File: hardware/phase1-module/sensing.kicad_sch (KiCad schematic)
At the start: 0 parts

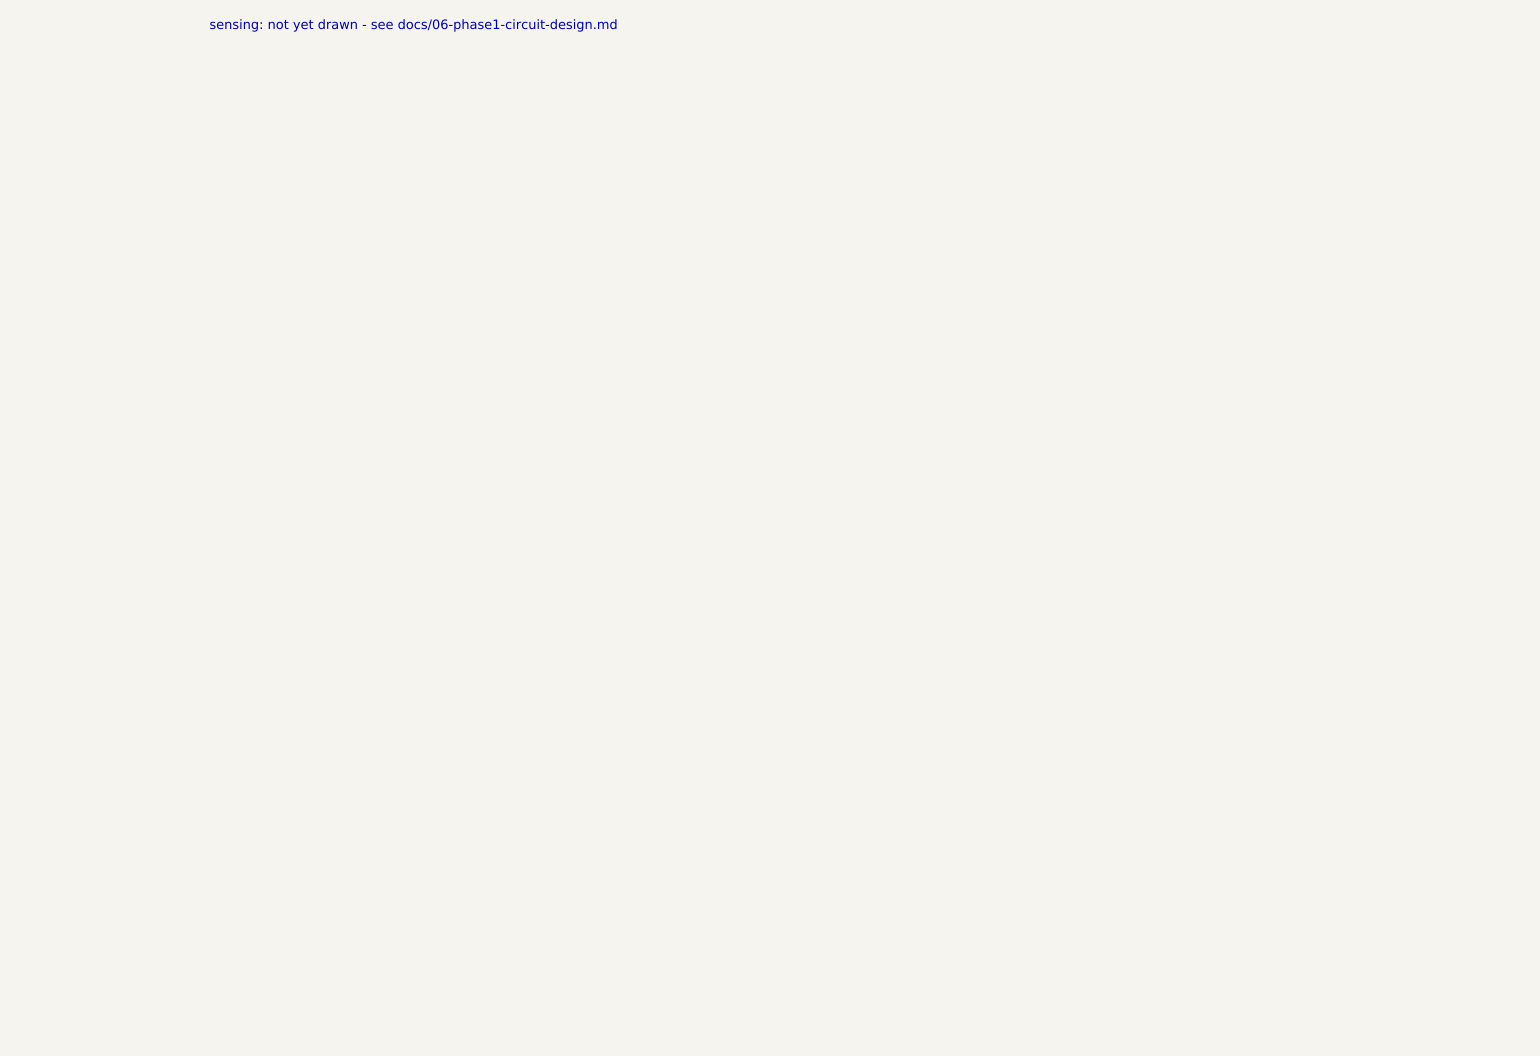
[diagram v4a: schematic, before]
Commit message: Complete Phase-1 schematic: all six remaining sheets, netlist-verified
- power-stage: LM5145 @350kHz (RT 28.7K per ds eq.3), RDS(on) valley
  ILIM 365R->SW, UVLO divider, EN kill chain (NOT(HW_EN) OR PS_OFF via
  Q5/Q6 + diode-OR), Type-III comp starting values, SYNCIN as DEM/FPWM
- sensing: 2m shunt, INA240A3 -> CC loop, INA228 telemetry, /8 divider,
  NT1 single AGND-PGND tie
- disconnect: back-to-back FETs + LTC7004, INP = OUT_REQ AND NOT(kill)
  AND NOT(OVP); TLV7011 + Q9 trips at 22.25V
- aux-rails: LMR36015 (5.016V) -> NCP1117 3V3
- mcu-can: STM32G431CBT6 fully pinned; I2C moved to I2C2/PA8-PA9 (PB8
  is the BOOT0 strap - pullup there would boot the ROM loader), BOOT0
  strapped low, OUT_REQ on PB14 (PB4 NJTRST reset pull-up), 8MHz
  crystal for CAN, TCAN1042 (VCC 5V, VIO 3V3)
- io: fused input + SMBJ33A TVS, output, backplane header, fan switch
  (1N4148W flyback orientation corrected: pin 1 = cathode)
- checker: duplicate-ref detection + global/local split-net detection;
  caught duplicate C62 and the LMR36015 FB-pin placement collision

Co-Authored-By: Claude Fable 5 <noreply@anthropic.com>
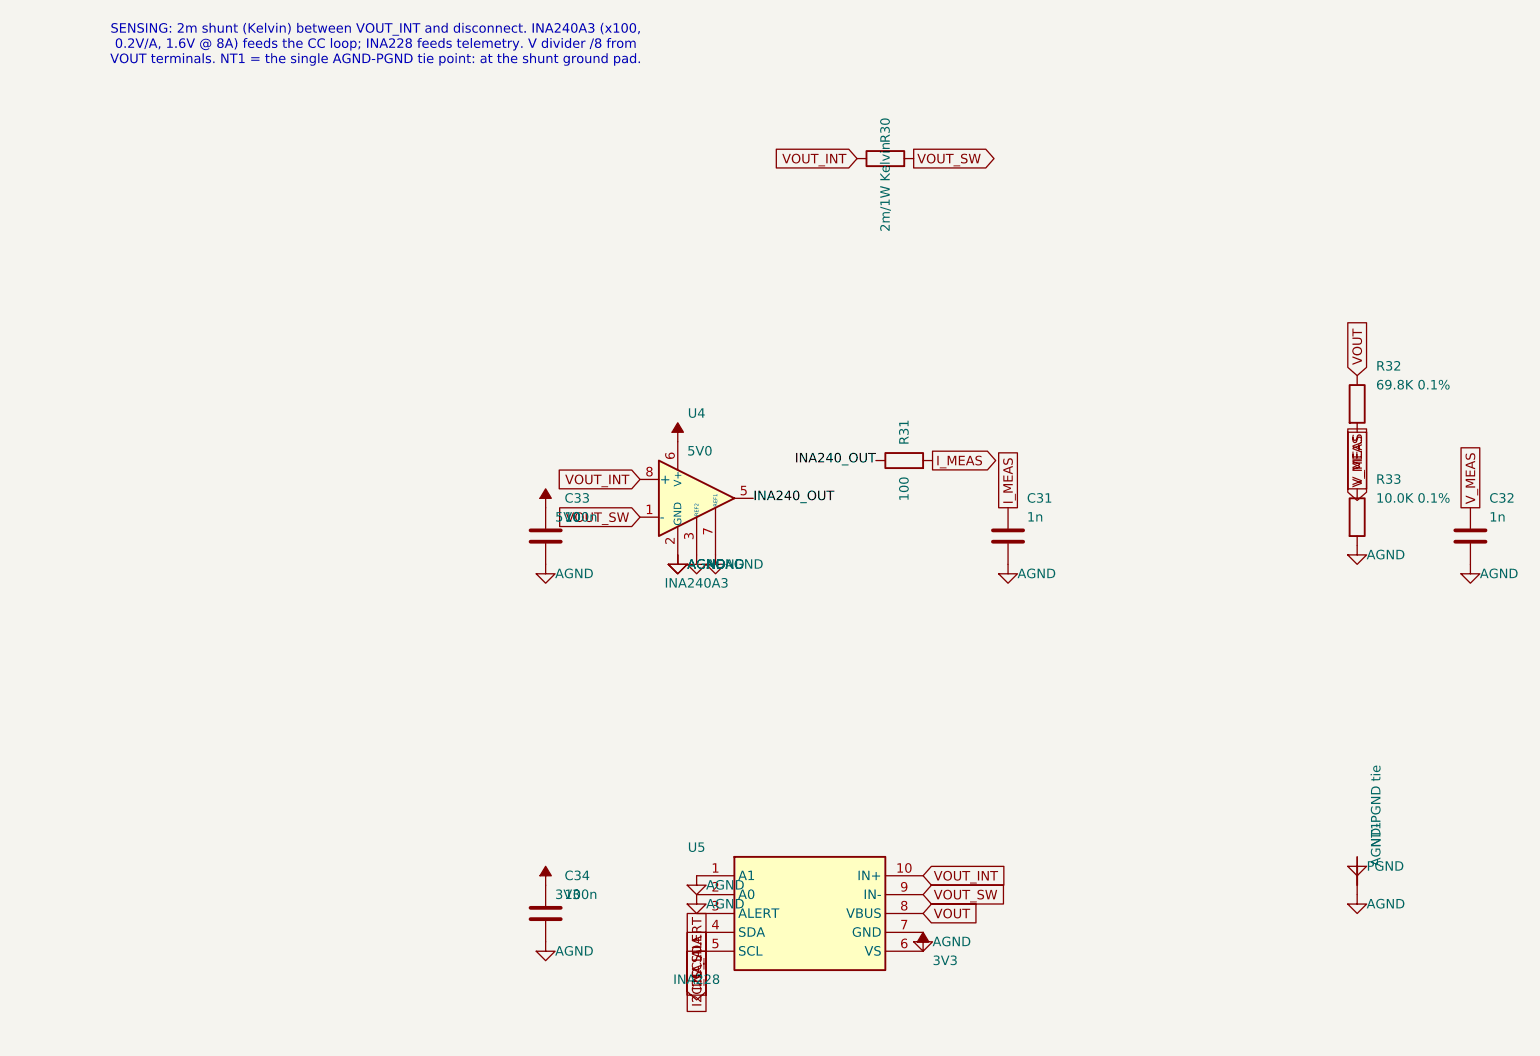
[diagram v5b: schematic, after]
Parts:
- added C31, C32: 1n, Capacitor_SMD:C_0402_1005Metric, symbol Device:C
- added C33, C34: 100n, Capacitor_SMD:C_0402_1005Metric, symbol Device:C
- added NT1: AGND-PGND tie, symbol Device:NetTie_2
- added R30: 2m/1W Kelvin, Resistor_SMD:R_2512_6332Metric, symbol Device:R
- added R31: 100, Resistor_SMD:R_0402_1005Metric, symbol Device:R
- added R32: 69.8K 0.1%, Resistor_SMD:R_0402_1005Metric, symbol Device:R
- added R33: 10.0K 0.1%, Resistor_SMD:R_0402_1005Metric, symbol Device:R
- added U4: INA240A3, Package_SO:SOIC-8_3.9x4.9mm_P1.27mm, symbol Amplifier_Current:INA240A3D
- added U5: INA228, Package_SO:VSSOP-10_3x3mm_P0.5mm, symbol labbench:INA228AIDGSR
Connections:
- new net 3V3: C34.1, U5.6 (VS)
- new net 5V0: C33.1, U4.6 (V+)
- new net AGND: C31.2, C32.2, C33.2, C34.2, NT1.1, R33.2, U4.2 (GND), U4.3 (REF2), U4.4 (GND), U4.7 (REF1), U5.1 (A1), U5.2 (A0), U5.7 (GND)
- new net I2C_SCL: U5.5 (SCL)
- new net I2C_SDA: U5.4 (SDA)
- new net INA240_OUT: R31.1, U4.5
- new net INA_ALERT: U5.3 (ALERT)
- new net I_MEAS: C31.1, R31.2
- new net PGND: NT1.2
- new net VOUT: R32.1, U5.8 (VBUS)
- new net VOUT_INT: R30.1, U4.8 (+), U5.10 (IN+)
- new net VOUT_SW: R30.2, U4.1 (-), U5.9 (IN-)
- new net V_MEAS: C32.1, R32.2, R33.1
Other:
- note added: "SENSING: 2m shunt (Kelvin) between VOUT_INT and disconnect. INA240A3 (x100, 0.2V/A, 1.6V @ 8A) feeds the CC loop; INA228 feeds telemetry. V divider /8 from VOUT terminals. NT1 = the single AGND-PGND tie point: at the shunt ground pad."
- note removed: "sensing: not yet drawn - see docs/06-phase1-circuit-design.md"

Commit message: Footprint pass: labbench.pretty library, all 137 components verified
- build_fplib.py: merges vetted vendor footprints (LM5145 RGY0020B,
  LMR36015 RNX, DAC80502 WSON-10 no-EP) and generates PowerFET_SON5x6_GDS
  from the TI Q5A land pattern (CSD18563Q5A SLPS444C) with pads renumbered
  1=G/2=D/3=S to match the generic NMOS symbol; writes fp-lib-table.
- check_footprints.py: every component must have a resolvable footprint and
  every netted pin a matching pad (caught a wrong official VSSOP-8 name).
- gen_phase1.py: passives 0402->0603 (hand assembly); DAC80502 vendor fp
  (DRX has no exposed pad); L1 = Coilcraft XAL1350-103ME on official fp;
  net-tie fp; crystal -> Crystal_GND24 with grounded shield pads; bulk cap
  banks expanded to one component per physical cap (C75-C81); R27 preload
  1W -> 2512.
- PARTS-TO-DOWNLOAD.md section D: new orderables for the footprint pass.

check_netlist + check_footprints: all OK (137 components).

Co-Authored-By: Claude Fable 5 <noreply@anthropic.com>
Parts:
- C31, C32, C33, C34: footprint Capacitor_SMD:C_0402_1005Metric -> Capacitor_SMD:C_0603_1608Metric
- NT1: footprint (none) -> NetTie:NetTie-2_SMD_Pad0.5mm
- R31, R32, R33: footprint Resistor_SMD:R_0402_1005Metric -> Resistor_SMD:R_0603_1608Metric

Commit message: PCB placement v1 + kicad-happy audit fixes
gen_board.py: netlist-driven board generator (120x80 4-layer) — placement
table for all 137 components, split In1 ground plane (PGND/AGND star at
NT1, AGND pocket under the LTC7004 cluster), In2 5V0/3V3 distribution,
9 F.Cu power pours with straddled cap banks, mechanical checks (pad-in-pour
assertions, courtyard overlap/edge detection). run_drc.py wraps pcbnew
WriteDRCReport (KiCad 7 has no CLI drc).

Audit (kicad-happy analyzers: schematic+PCB+cross+EMC+thermal) fixes:
- R31 100R -> 1K: INA240 rails at ~4.8V on the 5V rail during OC transients;
  PA1 is TT_a (3.6V) — 100R allowed ~12mA clamp injection vs 5mA abs max
- C43 moved to decouple U7 (was 21mm away), C50/C51 tight to U8 VIN
  (hot-loop), SW pour trimmed north (radiating area), 3 fiducials added,
  H2 courtyard off the board edge

Co-Authored-By: Claude Fable 5 <noreply@anthropic.com>
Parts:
- R31: value 100 -> 1K
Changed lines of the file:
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@@
     (in_bom yes) (on_board yes) (dnp no)
     (property "Reference" "R31" (at 104.14 92.71 0) (effects (font (size 1.27 1.27))))
-    (property "Value" "100" (at 104.14 100.33 0) (effects (font (size 1.27 1.27))))
+    (property "Value" "1K" (at 104.14 100.33 0) (effects (font (size 1.27 1.27))))
     (property "Footprint" "Resistor_SMD:R_0603_1608Metric" (at 104.14 96.52 0) (effects (font (size 1.27 1.27)) hide))
     (property "Datasheet" "~" (at 104.14 96.52 0) (effects (font (size 1.27 1.27)) hide))
